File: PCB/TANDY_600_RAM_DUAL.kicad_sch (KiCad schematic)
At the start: 8 parts, among them CN1 TANDY_600_RAM_BUS_plain_pins, CN2 TANDY_600_RAM_BUS_plain_pins, U1 AS6C2008A, U2 HC148, U3 1G02

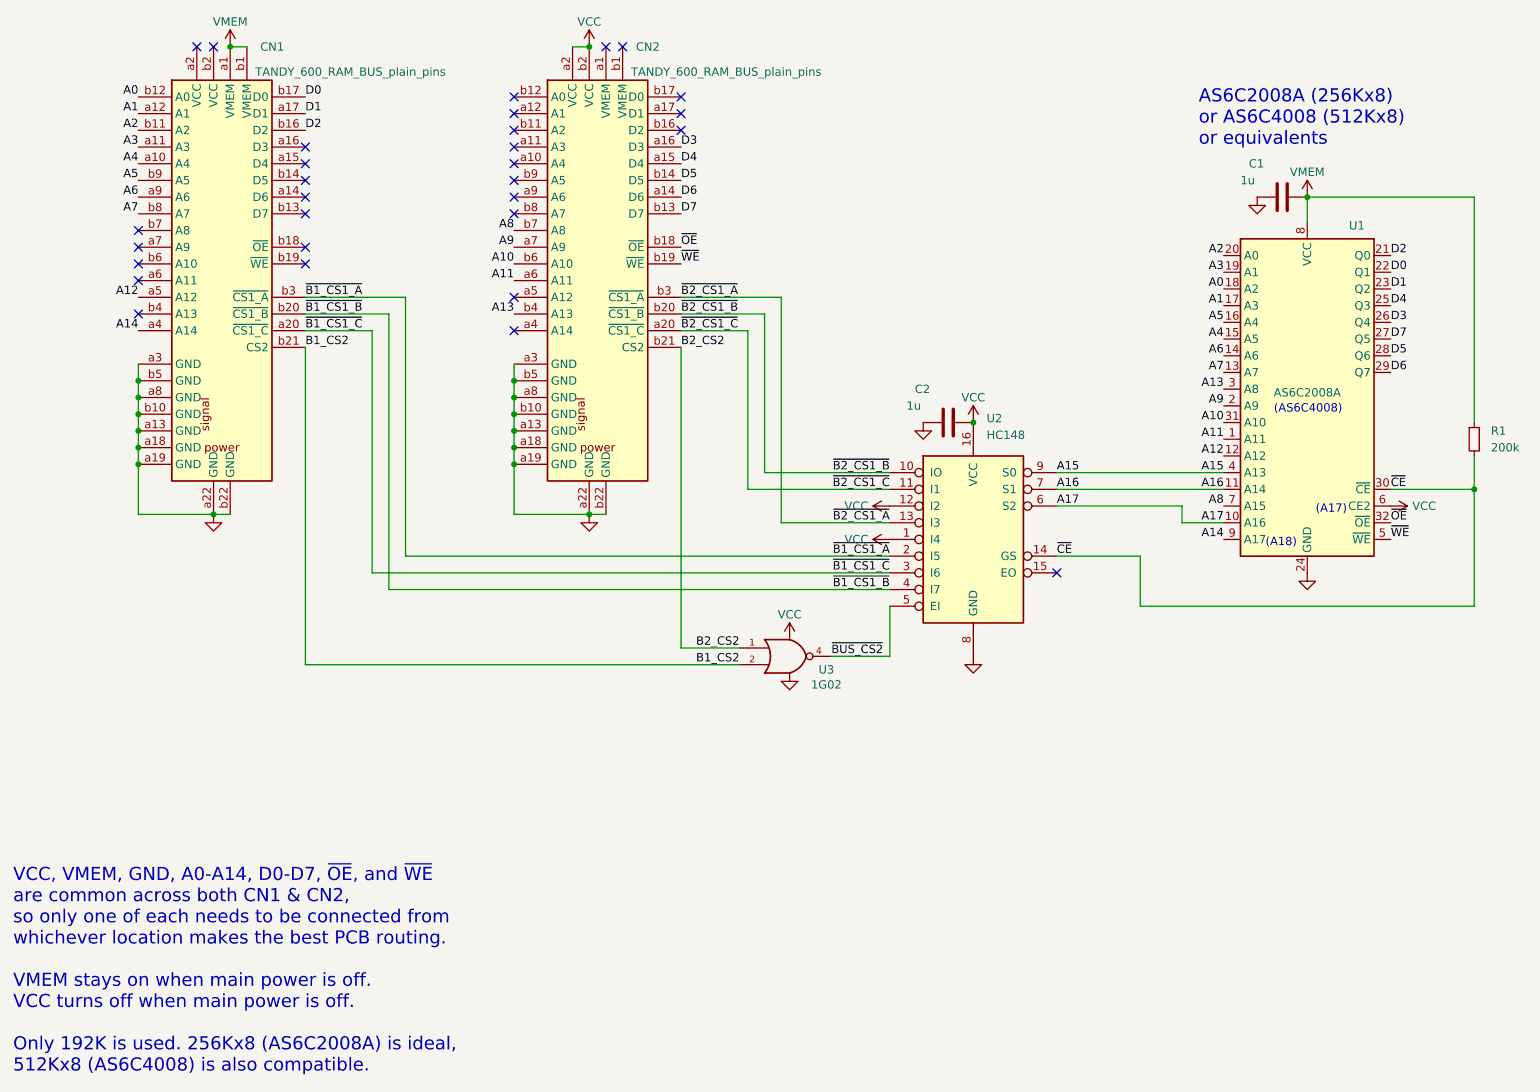
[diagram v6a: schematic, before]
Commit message: dual: relocate chips for shorter traces & fewer vias, add service manual
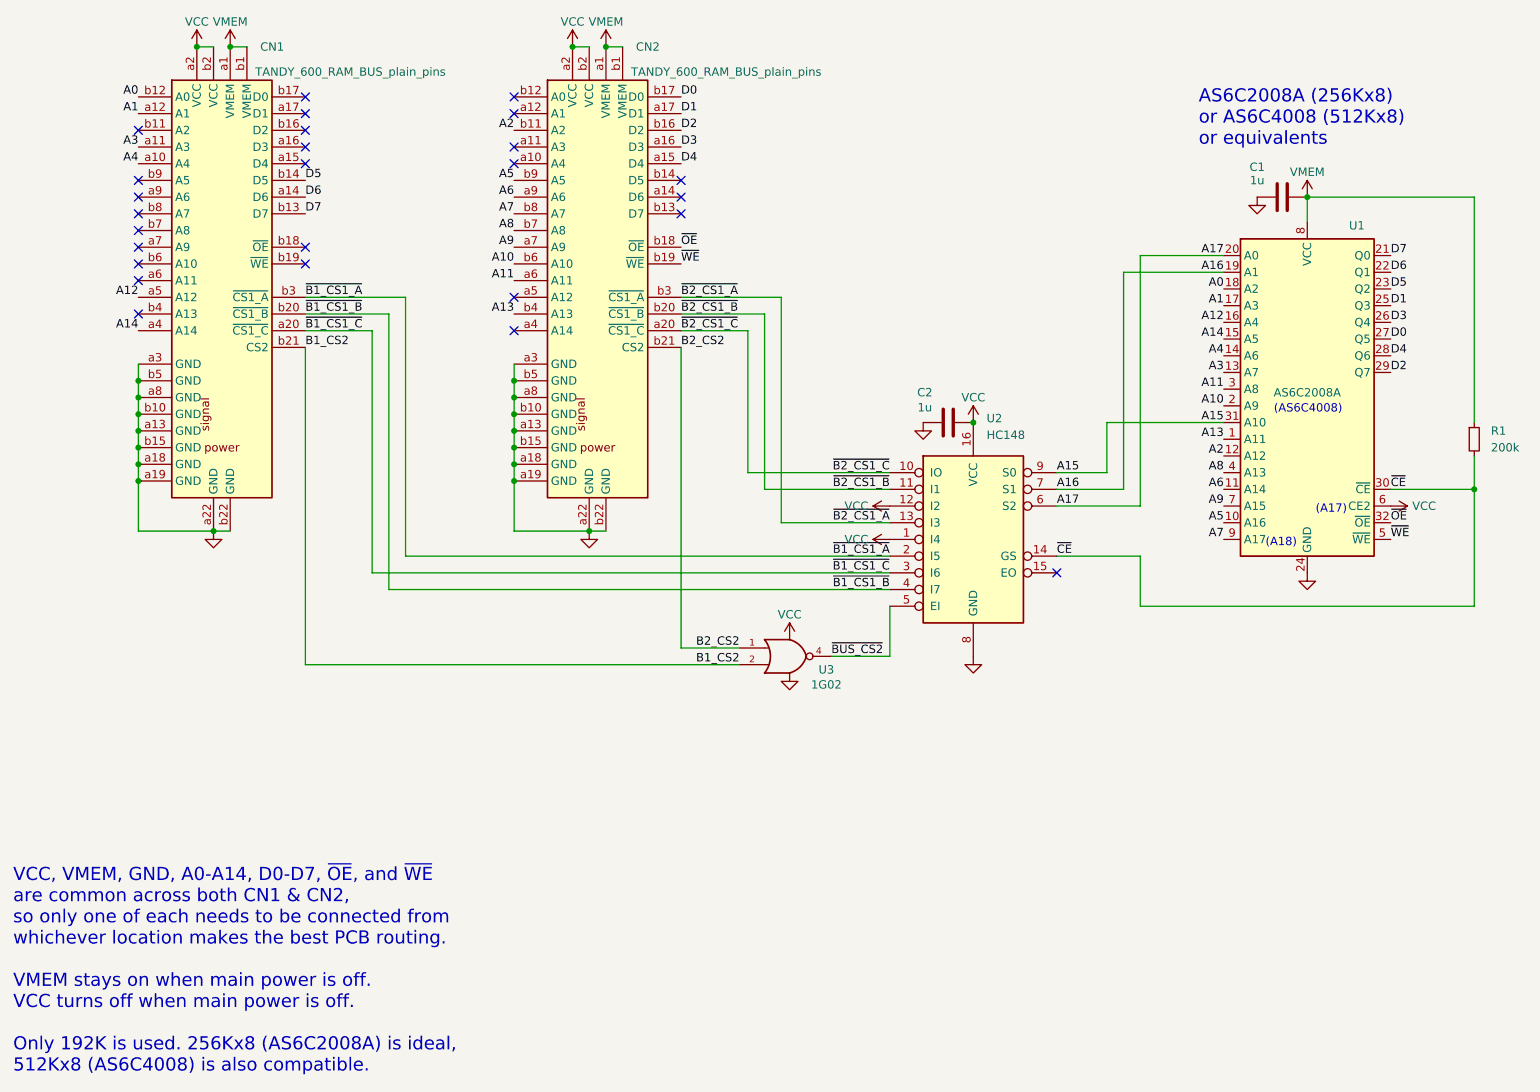
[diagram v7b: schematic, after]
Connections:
- net A10: now also U1.2 (A9); no longer U1.31 (A10)
- net A11: now also U1.3 (A8); no longer U1.1 (A11)
- net A12: now also U1.16 (A4); no longer U1.12 (A12)
- net A13: now also U1.1 (A11); no longer U1.3 (A8)
- net A14: now also U1.15 (A5); no longer U1.9 (A17)
- net A15: now also U1.31 (A10); no longer U1.4 (A13)
- net A16: now also U1.19 (A1); no longer U1.11 (A14)
- net A17: now also U1.20 (A0); no longer U1.10 (A16)
- net A2: now also CN2.b11 (A2), U1.12 (A12); no longer CN1.b11 (A2), U1.20 (A0)
- net A3: now also U1.13 (A7); no longer U1.19 (A1)
- net A4: now also U1.14 (A6); no longer U1.15 (A5)
- net A5: now also CN2.b9 (A5), U1.10 (A16); no longer CN1.b9 (A5), U1.16 (A4)
- net A6: now also CN2.a9 (A6), U1.11 (A14); no longer CN1.a9 (A6), U1.14 (A6)
- net A7: now also CN2.b8 (A7), U1.9 (A17); no longer CN1.b8 (A7), U1.13 (A7)
- net A8: now also U1.4 (A13); no longer U1.7 (A15)
- net A9: now also U1.7 (A15); no longer U1.2 (A9)
- net D0: now also CN2.b17 (D0), U1.27 (Q5); no longer CN1.b17 (D0), U1.22 (Q1)
- net D1: now also CN2.a17 (D1), U1.25 (Q3); no longer CN1.a17 (D1), U1.23 (Q2)
- net D2: now also CN2.b16 (D2), U1.29 (Q7); no longer CN1.b16 (D2), U1.21 (Q0)
- net D4: now also U1.28 (Q6); no longer U1.25 (Q3)
- net D5: now also CN1.b14 (D5), U1.23 (Q2); no longer CN2.b14 (D5), U1.28 (Q6)
- net D6: now also CN1.a14 (D6), U1.22 (Q1); no longer CN2.a14 (D6), U1.29 (Q7)
- net D7: now also CN1.b13 (D7), U1.21 (Q0); no longer CN2.b13 (D7), U1.27 (Q5)
- net GND: now also CN1.b15 (GND), CN2.b15 (GND)
- net VCC: now also CN1.a2 (VCC), CN1.b2 (VCC)
- net VMEM: now also CN2.a1 (VMEM), CN2.b1 (VMEM)
- net ~{B2_CS1_B}: now also U2.11 (I1); no longer U2.10 (IO)
- net ~{B2_CS1_C}: now also U2.10 (IO); no longer U2.11 (I1)
- no-connect marks 30 -> 26
